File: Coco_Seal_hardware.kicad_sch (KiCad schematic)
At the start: 10 parts, among them P1 USB_C_Plug_USB2.0, SW1 SW_Push_Dual, U1 ESP32-C3-WROOM-02-N4, U2 E220-900T22S（JP）-EV2, U3 ESP32-C3-WROOM-02, U4 ER_OLEDM0.91_1x-I2C, U5 TPSM53602RDA, U6 LTC4055

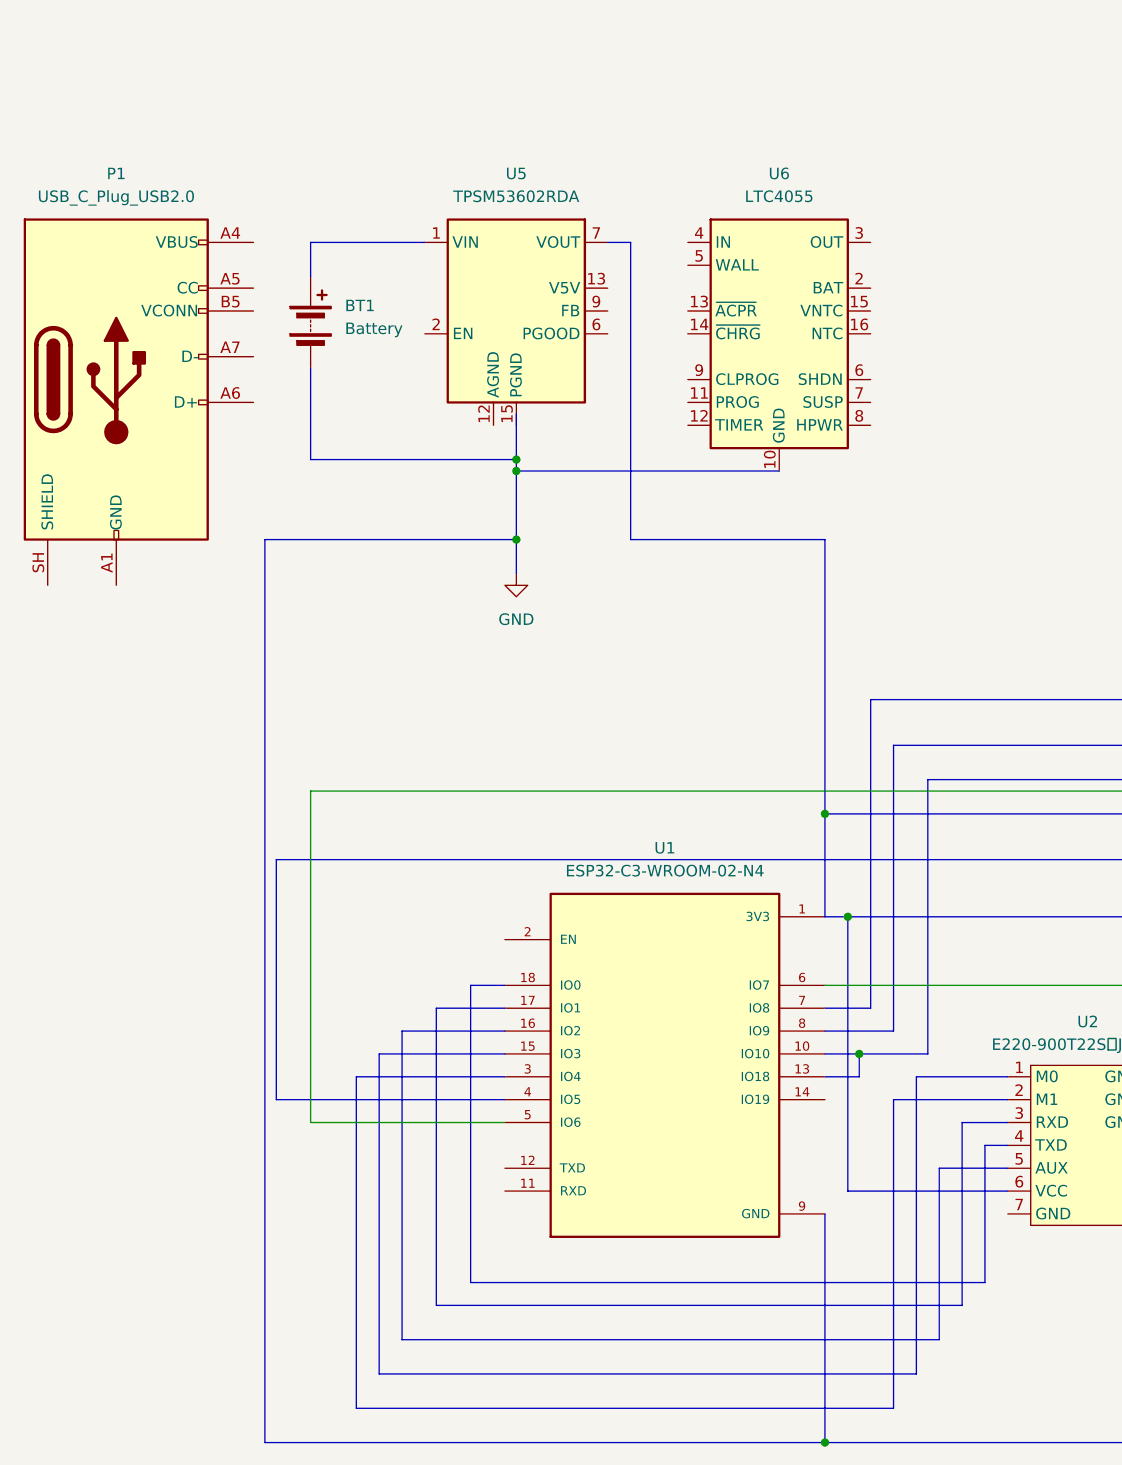
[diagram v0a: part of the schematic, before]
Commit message: vccを配線した
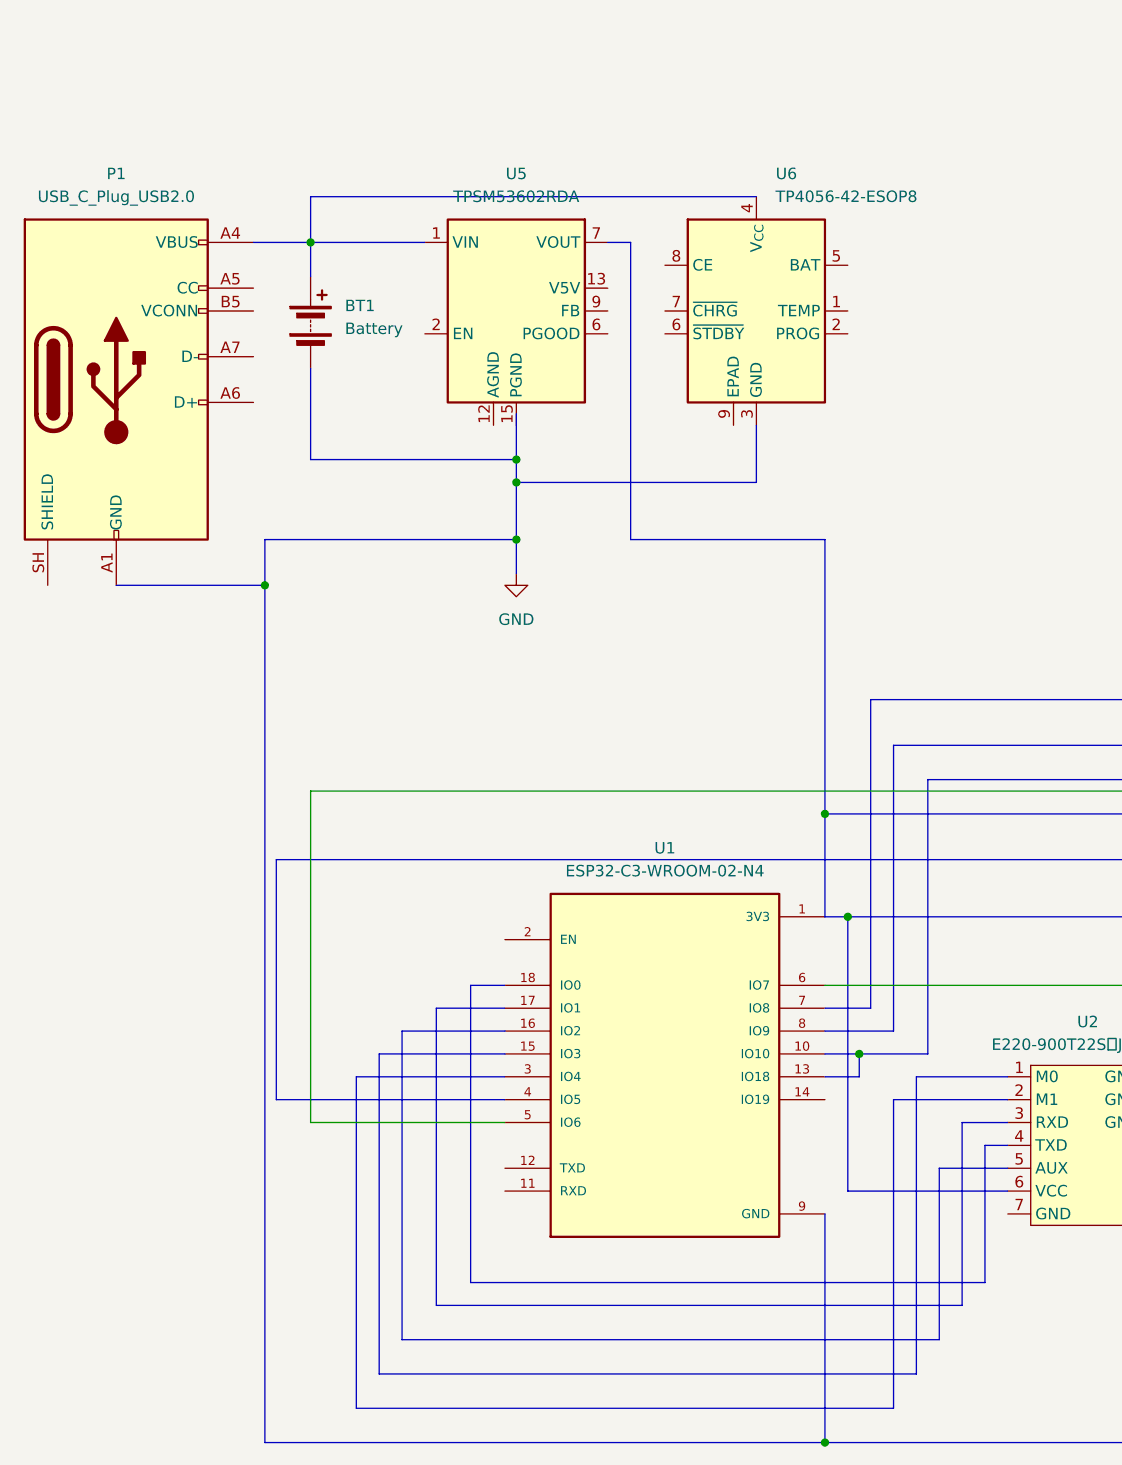
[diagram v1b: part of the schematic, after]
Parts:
- removed U6: LTC4055, Package_DFN_QFN:QFN-16-1EP_4x4mm_P0.65mm_EP2.15x2.15mm, symbol Battery_Management:LTC4055
- added U6: TP4056-42-ESOP8, Package_SO:SOIC-8-1EP_3.9x4.9mm_P1.27mm_EP2.41x3.3mm_ThermalVias, symbol Battery_Management:TP4056-42-ESOP8
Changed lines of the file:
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@@
 	)
 	(junction
-		(at 85.09 81.28)
+		(at 57.15 93.98)
 		(diameter 0)
 		(color 0 0 0 0)
@@
 	)
 	(junction
+		(at 85.09 82.55)
+		(diameter 0)
+		(color 0 0 0 0)
+	)
+	(junction
 		(at 179.07 115.57)
 		(diameter 0)
@@
 	)
 	(junction
+		(at 62.23 55.88)
+		(diameter 0)
+		(color 0 0 0 0)
+	)
+	(junction
 		(at 123.19 146.05)
 		(diameter 0)
@@
 	(bus
 		(pts
+			(xy 111.76 82.55) (xy 85.09 82.55)
+		)
+		(stroke
+			(width 0)
+			(type default)
+		)
+	)
+	(bus
+		(pts
 			(xy 119.38 130.81) (xy 119.38 119.38)
 		)
@@
 	(bus
 		(pts
+			(xy 57.15 93.98) (xy 57.15 88.9)
+		)
+		(stroke
+			(width 0)
+			(type default)
+		)
+	)
+	(bus
+		(pts
 			(xy 127 151.13) (xy 139.7 151.13)
 		)
@@
 	(bus
 		(pts
+			(xy 111.76 76.2) (xy 111.76 82.55)
+		)
+		(stroke
+			(width 0)
+			(type default)
+		)
+	)
+	(bus
+		(pts
 			(xy 119.38 119.38) (xy 168.91 119.38)
 		)
@@
 		)
 	)
+	(bus
+		(pts
+			(xy 62.23 50.8) (xy 62.23 55.88)
+		)
+		(stroke
+			(width 0)
+			(type default)
+		)
+	)
 	(wire
 		(pts
@@
 	(bus
 		(pts
-			(xy 85.09 81.28) (xy 114.3 81.28)
-		)
-		(stroke
-			(width 0)
-			(type default)
-		)
-	)
-	(bus
-		(pts
 			(xy 80.01 138.43) (xy 80.01 171.45)
 		)
@@
 	(bus
 		(pts
-			(xy 85.09 80.01) (xy 85.09 88.9)
+			(xy 85.09 80.01) (xy 85.09 82.55)
 		)
 		(stroke
@@
 	(bus
 		(pts
+			(xy 111.76 50.8) (xy 62.23 50.8)
+		)
+		(stroke
+			(width 0)
+			(type default)
+		)
+	)
+	(bus
+		(pts
 			(xy 130.81 115.57) (xy 179.07 115.57)
 		)
@@
 	(bus
 		(pts
+			(xy 85.09 82.55) (xy 85.09 88.9)
+		)
+		(stroke
+			(width 0)
+			(type default)
+		)
+	)
+	(bus
+		(pts
+			(xy 40.64 93.98) (xy 57.15 93.98)
+		)
+		(stroke
+			(width 0)
+			(type default)
+		)
+	)
+	(bus
+		(pts
 			(xy 160.02 151.13) (xy 160.02 189.23)
 		)
@@
 	(bus
 		(pts
+			(xy 55.88 55.88) (xy 62.23 55.88)
+		)
+		(stroke
+			(width 0)
+			(type default)
+		)
+	)
+	(bus
+		(pts
 			(xy 62.23 80.01) (xy 85.09 80.01)
 		)
@@
 	(bus
 		(pts
-			(xy 57.15 189.23) (xy 57.15 88.9)
+			(xy 57.15 189.23) (xy 57.15 93.98)
 		)
 		(stroke
@@
 	)
 	(symbol
-		(lib_id "Battery_Management:LTC4055")
-		(at 114.3 66.04 0)
+		(lib_id "Battery_Management:TP4056-42-ESOP8")
+		(at 111.76 63.5 0)
 		(unit 1)
 		(body_style 1)
@@
 		(fields_autoplaced yes)
 		(property "Reference" "U6"
-			(at 114.3 48.26 0)
-			(show_name no)
-			(do_not_autoplace no)
-			(effects
-				(font
-					(size 1.27 1.27)
-				)
-			)
-		)
-		(property "Value" "LTC4055"
-			(at 114.3 50.8 0)
-			(show_name no)
-			(do_not_autoplace no)
-			(effects
-				(font
-					(size 1.27 1.27)
-				)
-			)
-		)
-		(property "Footprint" "Package_DFN_QFN:QFN-16-1EP_4x4mm_P0.65mm_EP2.15x2.15mm"
-			(at 114.3 88.9 0)
-			(hide yes)
-			(show_name no)
-			(do_not_autoplace no)
-			(effects
-				(font
-					(size 1.27 1.27)
-				)
-			)
-		)
-		(property "Datasheet" "https://www.analog.com/media/en/technical-documentation/data-sheets/4055fb.pdf"
-			(at 114.3 78.74 0)
-			(hide yes)
-			(show_name no)
-			(do_not_autoplace no)
-			(effects
-				(font
-					(size 1.27 1.27)
-				)
-			)
-		)
-		(property "Description" "USB Power Controller and Li-Ion Charger (4.2V Float Voltage)"
-			(at 114.3 66.04 0)
-			(hide yes)
-			(show_name no)
-			(do_not_autoplace no)
-			(effects
-				(font
-					(size 1.27 1.27)
-				)
-			)
-		)
-		(pin "13"
-		)
-		(pin "15"
-		)
-		(pin "16"
-		)
-		(pin "14"
-		)
-		(pin "12"
-		)
-		(pin "17"
+			(at 113.9033 48.26 0)
+			(show_name no)
+			(do_not_autoplace no)
+			(effects
+				(font
+					(size 1.27 1.27)
+				)
+				(justify left)
+			)
+		)
+		(property "Value" "TP4056-42-ESOP8"
+			(at 113.9033 50.8 0)
+			(show_name no)
+			(do_not_autoplace no)
+			(effects
+				(font
+					(size 1.27 1.27)
+				)
+				(justify left)
+			)
+		)
+		(property "Footprint" "Package_SO:SOIC-8-1EP_3.9x4.9mm_P1.27mm_EP2.41x3.3mm_ThermalVias"
+			(at 112.268 86.36 0)
+			(hide yes)
+			(show_name no)
+			(do_not_autoplace no)
+			(effects
+				(font
+					(size 1.27 1.27)
+				)
+			)
+		)
+		(property "Datasheet" "https://www.lcsc.com/datasheet/lcsc_datasheet_2410121619_TOPPOWER-Nanjing-Extension-Microelectronics-TP4056-42-ESOP8_C16581.pdf"
+			(at 111.76 88.9 0)
+			(hide yes)
+			(show_name no)
+			(do_not_autoplace no)
+			(effects
+				(font
+					(size 1.27 1.27)
+				)
+			)
+		)
+		(property "Description" "1A Standalone Linear Li-ion/LiPo single-cell battery charger, 4.2V ±1% charge voltage, VCC = 4.0..8.0V, SOIC-8 (SOP-8)"
+			(at 112.268 83.82 0)
+			(hide yes)
+			(show_name no)
+			(do_not_autoplace no)
+			(effects
+				(font
+					(size 1.27 1.27)
+				)
+			)
 		)
 		(pin "6"
 		)
+		(pin "5"
+		)
+		(pin "1"
+		)
+		(pin "2"
+		)
+		(pin "3"
+		)
+		(pin "4"
+		)
 		(pin "7"
 		)
 		(pin "9"
 		)
-		(pin "2"
-		)
-		(pin "10"
-		)
-		(pin "3"
-		)
-		(pin "5"
-		)
-		(pin "11"
-		)
-		(pin "1"
-		)
 		(pin "8"
 		)
-		(pin "4"
-		)
 		(instances

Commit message: README更新, 回路図更新
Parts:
- removed P1: USB_C_Plug_USB2.0, symbol Connector:USB_C_Plug_USB2.0
- removed U3: ESP32-C3-WROOM-02, RF_Module:ESP32-C3-WROOM-02, symbol RF_Module:ESP32-C3-WROOM-02
- removed U5: TPSM53602RDA, Package_DFN_QFN:Texas_B3QFN-14-1EP_5x5.5mm_P0.65mm_ThermalVia, symbol Converter_DCDC:TPSM53602RDA
- added J1: USB_C_Receptacle_USB2.0_14P, symbol Connector:USB_C_Receptacle_USB2.0_14P
- added Q1: Q_Dual_NMOS_S1G1D2S2G2D1, Package_TO_SOT_SMD:SOT-23-6, symbol Transistor_FET:Q_Dual_NMOS_S1G1D2S2G2D1
- added R1, R2: 5.1K, symbol Device:R
- added U3: DW01A, Package_TO_SOT_SMD:SOT-23-6, symbol Battery_Management:DW01A
- added U5: AP2112K-3.3, Package_TO_SOT_SMD:SOT-23-5, symbol Regulator_Linear:AP2112K-3.3
- added U7: TPD2EUSB30A, Package_TO_SOT_SMD:Texas_DRT-3, symbol Power_Protection:TPD2EUSB30A
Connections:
- net GND: now also J1.A1 (GND), J1.A12 (GND), J1.B1 (GND), J1.B12 (GND), J1.SH (SHIELD), R1.2, R2.2, U7.3 (GND)
- net GPIO10: now reaches U1.10 (IO10)
- net GPIO10: now also U2.5 (AUX)
- net UART_RXD: now reaches U1.11 (RXD)
- net UART_RXD: now also U2.4 (TXD)
- net UART_TXD: now reaches U1.12 (TXD)
- net UART_TXD: now also U2.3 (RXD)
- net GPIO18: now reaches U1.13 (IO18)
- net GPIO18: now also J1.A7 (D-), J1.B7 (D-), U7.2 (D-)
- net GPIO19: now reaches U1.14 (IO19)
- net GPIO19: now also J1.A6 (D+), J1.B6 (D+), U7.1 (D+)
- net GPIO3: now reaches U1.15 (IO3)
- net GPIO2: now reaches U1.16 (IO2)
- net GPIO1: now reaches U1.17 (IO1)
- net GPIO0: now reaches U1.18 (IO0)
- net GPIO4: now reaches U1.3 (IO4)
- net GPIO4: now also U4.4 (SDA)
- net GPIO5: now reaches U1.4 (IO5)
- net GPIO5: now also U4.3 (SCL)
- net GPIO6: now reaches U1.5 (IO6)
- net GPIO6: now also U2.2 (M1); no longer U4.4 (SDA)
- net GPIO7: now reaches U1.6 (IO7)
- net GPIO7: now also U2.1 (M0); no longer U4.3 (SCL)
- net GPIO8: now reaches U1.7 (IO8)
- net GPIO9: now reaches U1.8 (IO9)
- new net: J1.A4 (VBUS), J1.A9 (VBUS), J1.B4 (VBUS), J1.B9 (VBUS)
- new net: J1.A5 (CC1), R1.1
- new net: J1.B5 (CC2), R2.1
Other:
- moved on the sheet: BT1, BZ1, SW1, U1, U2, U4, U6

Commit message: 保護回路
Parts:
- removed BT1: Battery, symbol Device:Battery
- added BT1: Battery_Cell, symbol Device:Battery_Cell
- added C1: 0.1μF, symbol Device:C
- added R3: 1K, symbol Device:R
- added R4: 100, symbol Device:R
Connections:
- net at Q1.1 (S): now also U3.6 (GND), BT1.2 (-), C1.2
- net at Q1.2 (G): now also U3.1 (OD)
- net at Q1.6 (D): now also Q1.3 (D)
- net BATT-: now reaches Q1.4 (S)
- net BATT-: now also R3.2
- net at Q1.5 (G): now also U3.3 (OC)
- net at U3.2 (CS): now also R3.1
- net at U3.5 (VCC): now also C1.1, R4.2
- new net BATT+: BT1.1 (+), R4.1
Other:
- moved on the sheet: Q1A, Q1B, U3, U6

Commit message: 電源回路
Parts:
- removed Q1: Q_Dual_NMOS_S1G1D2S2G2D1, Package_TO_SOT_SMD:SOT-23-6, symbol Transistor_FET:Q_Dual_NMOS_S1G1D2S2G2D1
- removed U4: ER_OLEDM0.91_1x-I2C, Display:ER_OLEDM0.91_1x-I2C, symbol Display_Graphic:ER_OLEDM0.91_1x-I2C
- added C2, C3, C4: 10μF, symbol Device:C
- added C5: 1μF, symbol Device:C
- added C6: 0.1μF, symbol Device:C
- added Q1: FS8205A, Package_TO_SOT_SMD:SOT-23-6, symbol my_simbles:FS8205A
- added R5: 4.7K, symbol Device:R
- added R6: 10K, symbol Device:R
- added U8: SSD1306_OLED, symbol my_simbles:SSD1306_OLED
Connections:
- net BATT+ is gone; now on an unnamed net: BT1.1 (+), R4.1
- net BATT- is gone; now on net GND: R3.2
- net GND: now also U5.2 (GND), U6.1 (TEMP), U6.3 (GND), U6.6 (~{STDBY}), U6.7 (~{CHRG}), C2.2, C3.1, C4.2, C5.1, C6.2, Q1.3 (S2), R5.2
- net GPIO4: now also U8.4 (SDA)
- net GPIO5: now also U8.3 (SCK)
- net 3.3V: now reaches U1.1 (3V3)
- net 3.3V: now also U5.5 (VOUT), C4.1, C6.1, R6.2
- net at U1.2 (EN): now also C5.2, R6.1
- net at BT1.2 (-), C1.2, U3.6 (GND): now also Q1.1 (S1)
- net at U3.1 (OD): now also Q1.6 (G1)
- net at U3.3 (OC): now also Q1.4 (G2)
- net 5V: now reaches J1.A4 (VBUS), J1.A9 (VBUS), J1.B4 (VBUS), J1.B9 (VBUS)
- net 5V: now also U6.4 (V_{CC}), U6.8 (CE), C3.2
- net at U6.2 (PROG): now also R5.1
- net at U6.5 (BAT): now also U5.1 (VIN), U5.3 (EN), C2.1
- no-connect marks 0 -> 3
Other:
- moved on the sheet: BT1, C1, R3, R4, U1, U3, U5, U6

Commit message: 回路図いったん完成かな？
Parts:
- removed SW1: SW_Push_Dual, symbol Switch:SW_Push_Dual
- added C7: 0.1μF, symbol Device:C
- added D1: LED_Dual_KAK, symbol Device:LED_Dual_KAK
- added Q2: Q_NMOS, Package_TO_SOT_SMD:SOT-23, symbol Device:Q_NMOS
- added R10, R9: 10K, symbol Device:R
- added R11, R12: 330, symbol Device:R
- added R13: 100, symbol Device:R
- added R14, R7, R8: 100K, symbol Device:R
- added SW4, SW5, SW6: SW_Push, Button_Switch_THT:SW_PUSH_6mm, symbol Switch:SW_Push
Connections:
- net 3.3V: now also U2.6 (VCC), U8.2 (VDD), D1.2 (A), R10.1, R9.1
- net GND: now also BZ1.2 (-), U2.10 (GND), U2.7 (GND), U2.8 (GND), U2.9 (GND), U8.1 (GND), C7.1, R14.2, R8.2, SW4.1, SW5.1, SW6.1
- net GPIO0: now also C7.2, R7.2, R8.1
- net GPIO1: now also R9.2, SW4.2
- net GPIO2: now also R12.2
- net GPIO3: now also R13.1
- net GPIO8: now also R11.2
- net GPIO9: now also R10.2, SW5.2
- net at C5.2, R6.1, U1.2 (EN): now also SW6.2
- net BATT+: now reaches BT1.1 (+), C2.1, R4.1, U5.1 (VIN), U5.3 (EN), U6.5 (BAT)
- net BATT+: now also Q2.D, R7.1
- net at BZ1.1 (+): now also Q2.S
- new net: Q2.G, R13.2, R14.1
- new net Red: D1.3 (K2), R12.1
- new net Yellow-green: D1.1 (K1), R11.1
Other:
- moved on the sheet: BT1, BZ1, C1, C4, C5, C6, Q1, R3, R4, R6, U1, U3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

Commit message: コンデンサ追加
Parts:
- added C8: 10μF, symbol Device:C
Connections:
- net 3.3V: now also C8.1
- net GND: now also C8.2
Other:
- moved on the sheet: C6
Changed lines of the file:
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@@
 	)
 	(junction
+		(at 127 99.06)
+		(diameter 0)
+		(color 0 0 0 0)
+	)
+	(junction
 		(at 162.56 46.99)
 		(diameter 0)
@@
 	)
 	(junction
-		(at 118.11 99.06)
-		(diameter 0)
-		(color 0 0 0 0)
-	)
-	(junction
 		(at 139.7 62.23)
 		(diameter 0)
@@
 	)
 	(junction
+		(at 118.11 99.06)
+		(diameter 0)
+		(color 0 0 0 0)
+	)
+	(junction
 		(at 120.65 57.15)
 		(diameter 0)
@@
 	)
 	(junction
+		(at 134.62 99.06)
+		(diameter 0)
+		(color 0 0 0 0)
+	)
+	(junction
 		(at 143.51 179.07)
 		(diameter 0)
@@
 	(wire
 		(pts
-			(xy 119.38 99.06) (xy 118.11 99.06)
+			(xy 127 99.06) (xy 118.11 99.06)
 		)
 		(stroke
@@
 	(wire
 		(pts
+			(xy 134.62 86.36) (xy 134.62 99.06)
+		)
+		(stroke
+			(width 0)
+			(type default)
+		)
+	)
+	(wire
+		(pts
 			(xy 72.39 90.17) (xy 72.39 93.98)
 		)
@@
 	(wire
 		(pts
+			(xy 127 86.36) (xy 127 99.06)
+		)
+		(stroke
+			(width 0)
+			(type default)
+		)
+	)
+	(wire
+		(pts
 			(xy 95.25 39.37) (xy 95.25 31.75)
 		)
@@
 	(symbol
 		(lib_id "power:GND")
-		(at 127 99.06 0)
+		(at 134.62 99.06 0)
 		(unit 1)
 		(body_style 1)
@@
 		(fields_autoplaced yes)
 		(property "Reference" "#PWR010"
-			(at 127 105.41 0)
+			(at 134.62 105.41 0)
 			(hide yes)
 			(show_name no)
@@
 		)
 		(property "Value" "GND"
-			(at 127 104.14 0)
+			(at 134.62 104.14 0)
 			(show_name no)
 			(do_not_autoplace no)
@@
 		)
 		(property "Footprint" ""
-			(at 127 99.06 0)
+			(at 134.62 99.06 0)
 			(hide yes)
 			(show_name no)
@@
 		)
 		(property "Datasheet" ""
-			(at 127 99.06 0)
+			(at 134.62 99.06 0)
 			(hide yes)
 			(show_name no)
@@
 		)
 		(property "Description" "Power symbol creates a global label with name \"GND\" , ground"
-			(at 127 99.06 0)
+			(at 134.62 99.06 0)
 			(hide yes)
 			(show_name no)
@@
 	(symbol
 		(lib_id "Device:C")
-		(at 123.19 99.06 90)
+		(at 130.81 99.06 90)
 		(unit 1)
 		(body_style 1)
@@
 		(fields_autoplaced yes)
 		(property "Reference" "C6"
-			(at 123.19 91.44 90)
+			(at 130.81 91.44 90)
 			(show_name no)
 			(do_not_autoplace no)
@@
 		)
 		(property "Value" "0.1μF"
-			(at 123.19 93.98 90)
+			(at 130.81 93.98 90)
 			(show_name no)
 			(do_not_autoplace no)
@@
 		)
 		(property "Footprint" ""
-			(at 127 98.0948 0)
+			(at 134.62 98.0948 0)
 			(hide yes)
 			(show_name no)
@@
 		)
 		(property "Datasheet" ""
-			(at 123.19 99.06 0)
+			(at 130.81 99.06 0)
 			(hide yes)
 			(show_name no)
@@
 		)
 		(property "Description" "Unpolarized capacitor"
-			(at 123.19 99.06 0)
+			(at 130.81 99.06 0)
 			(hide yes)
 			(show_name no)
@@
 					(unit 1)
 				)
+			)
+		)
+	)
+	(symbol
+		(lib_id "Device:C")
+		(at 130.81 86.36 90)
+		(unit 1)
+		(body_style 1)
+		(exclude_from_sim no)
+		(in_bom yes)
+		(on_board yes)
+		(in_pos_files yes)
+		(dnp no)
+		(fields_autoplaced yes)
+		(property "Reference" "C8"
+			(at 130.81 78.74 90)
+			(show_name no)
+			(do_not_autoplace no)
+			(effects
+				(font
+					(size 1.27 1.27)
+				)
+			)
+		)
+		(property "Value" "10μF"
+			(at 130.81 81.28 90)
+			(show_name no)
+			(do_not_autoplace no)
+			(effects
+				(font
+					(size 1.27 1.27)
+				)
+			)
+		)
+		(property "Footprint" ""
+			(at 134.62 85.3948 0)
+			(hide yes)
+			(show_name no)
+			(do_not_autoplace no)
+			(effects
+				(font
+					(size 1.27 1.27)
+				)
+			)
+		)
+		(property "Datasheet" ""
+			(at 130.81 86.36 0)
+			(hide yes)
+			(show_name no)
+			(do_not_autoplace no)
+			(effects
+				(font
+					(size 1.27 1.27)
+				)
+			)
+		)
+		(property "Description" "Unpolarized capacitor"
+			(at 130.81 86.36 0)
+			(hide yes)
+			(show_name no)
+			(do_not_autoplace no)
+			(effects
+				(font
+					(size 1.27 1.27)
+				)
+			)
+		)
+		(pin "2"
+		)
+		(pin "1"
+		)
+		(instances
+			(project "Coco_Seal_hardware"
+				(path "/32cbe908-45a7-4343-8d65-8d0ee985ed0b"
+					(reference "C8")
+					(unit 1)
+				)
